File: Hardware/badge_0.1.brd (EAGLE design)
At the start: 100 x 50 mm, 59 parts, among them CON1 PH_2, IC1 CP2102, SW2 MK12C02, U1 SMBT2222A, U2 SMBT2222A, U4 MCP73832T-2DCI/OT

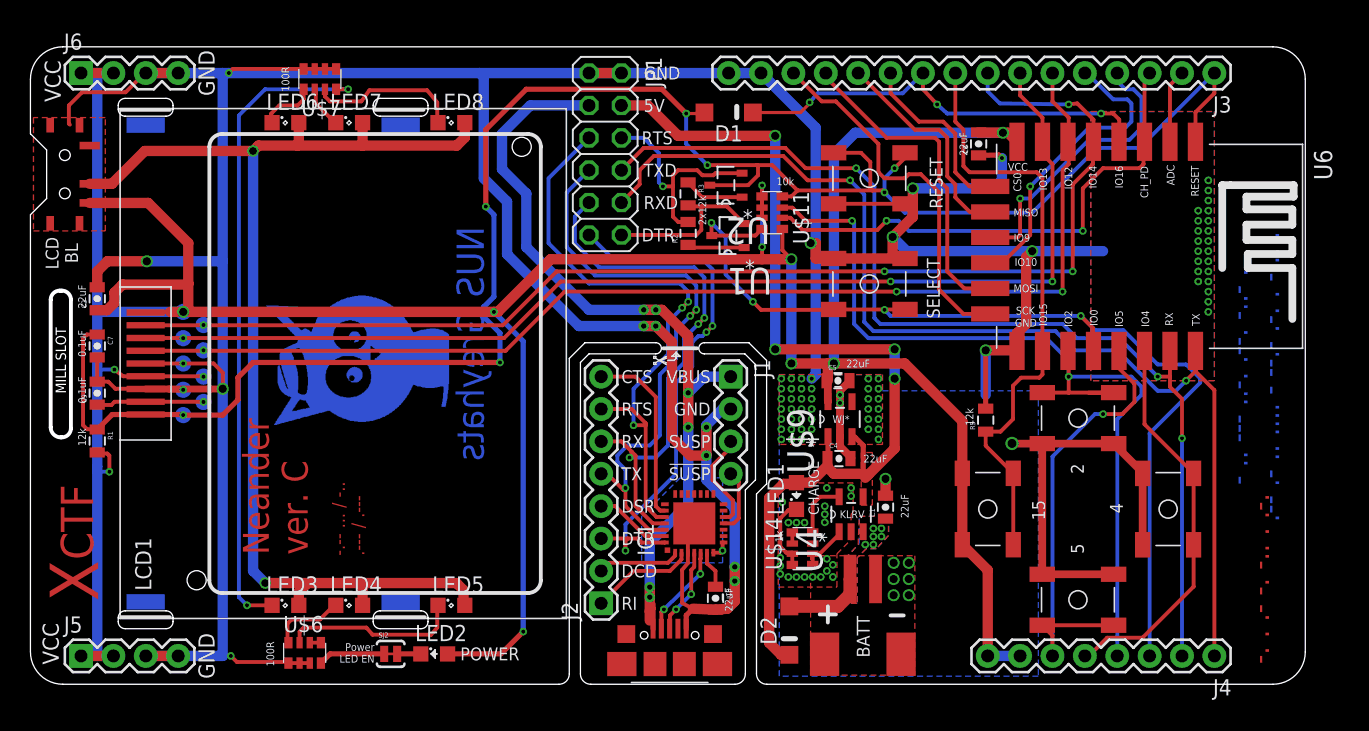
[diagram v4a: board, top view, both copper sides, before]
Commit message: Adjusted LCD mounting holes further apart for snug fit.
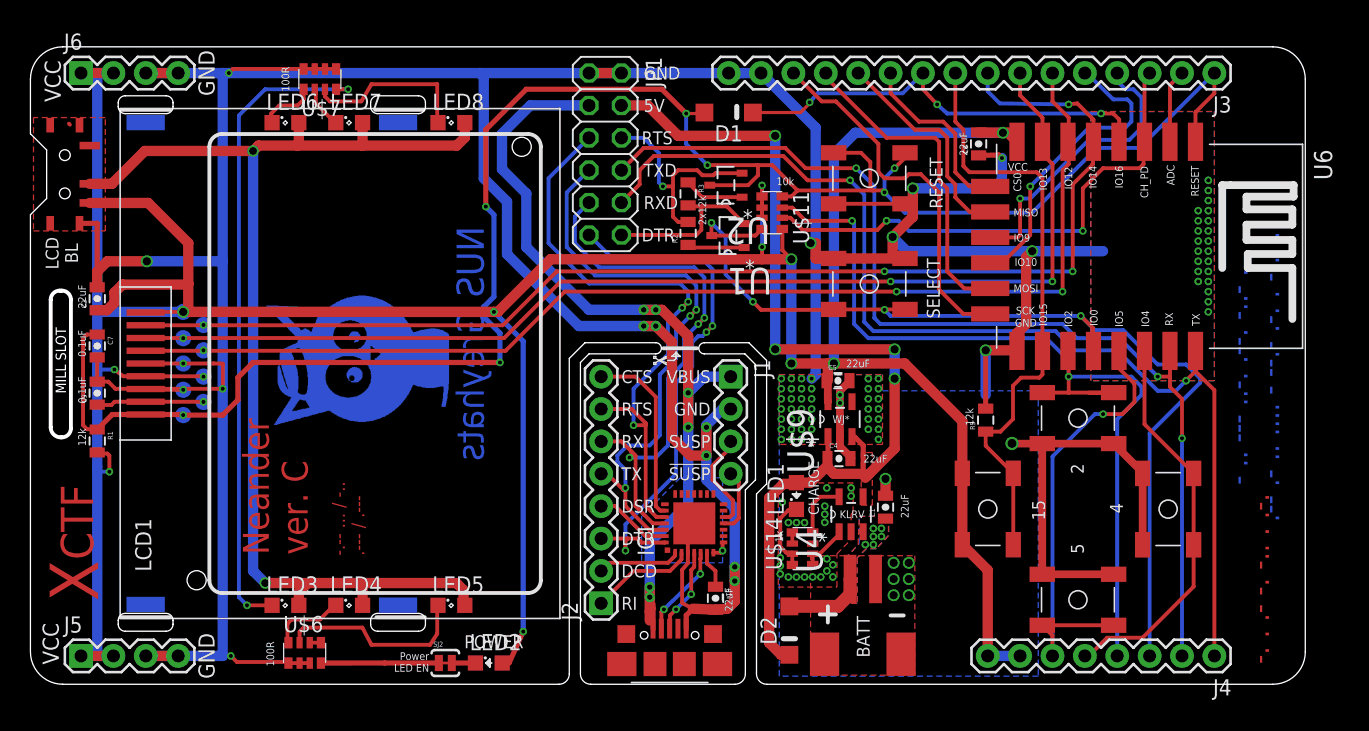
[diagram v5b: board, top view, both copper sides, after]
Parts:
- moved SJ2 4.35 mm to (32.5, 1.67)
- moved LED2 4.35 mm to (36.0, 1.67)
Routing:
- net N$15: track 5.26 -> 9.25 mm
- net VCC: track 277.7 -> 274.3 mm
- net N$8: track 12.0 -> 13.3 mm
- net N$13: track 14.1 -> 15.3 mm
